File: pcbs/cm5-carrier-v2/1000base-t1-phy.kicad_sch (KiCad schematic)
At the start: 55 parts, among them J1101 MSPE-J2L0-x00, U1101 LAN8870, Y1101 XRCGB25M000F3A16R0

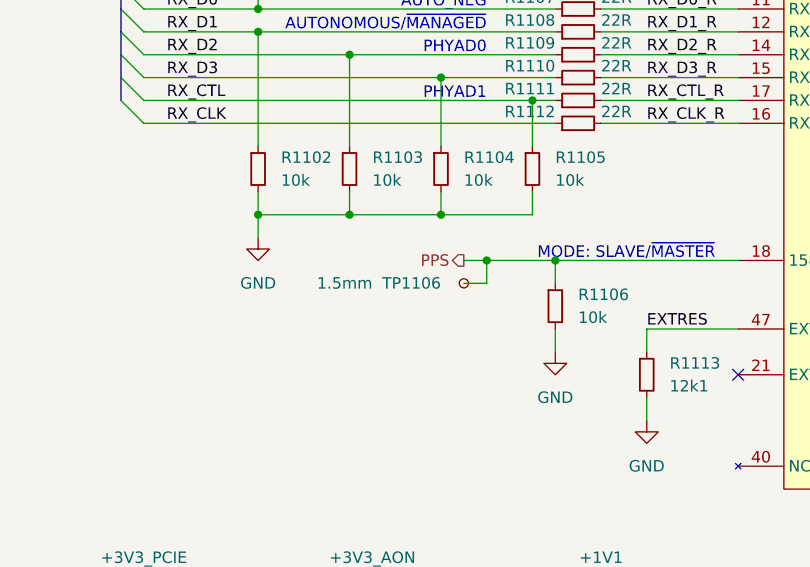
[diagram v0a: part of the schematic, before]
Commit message: Changed UART connector to I2C
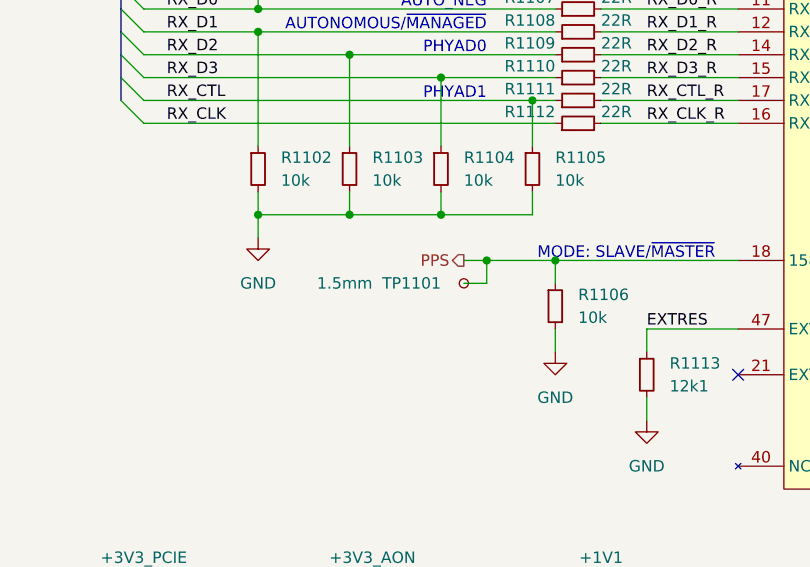
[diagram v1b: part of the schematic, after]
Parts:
- renumbered TP1106 to TP1101
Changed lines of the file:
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@@
 		(in_pos_files yes)
 		(dnp no)
-		(property "Reference" "TP1106"
+		(property "Reference" "TP1101"
 			(at 60.96 106.68 0)
 			(show_name no)
@@
 			(project "cm5-carrier-v2"
 				(path "/f91ec272-d09a-4038-bbbb-962739a92c51/760d12ad-9269-4cb7-9058-d98dd001df15"
-					(reference "TP1106")
+					(reference "TP1101")
 					(unit 1)
 				)
